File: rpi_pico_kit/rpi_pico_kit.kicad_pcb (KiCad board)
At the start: 2 copper layers, 99.1 x 99.1 mm, 195 parts, among them J1 DC Jack 5.5x2.1mm, J10 OLED Display SSD1306, J11 Conn_01x04_Male, J12 Conn_01x04_Male, J13 AudioJack-CUI-SJ-3523-SMT, J14 AudioJack-CUI-SJ-3523-SMT, J2 USB_B, J3 Conn_01x03_Male, J4 DB15_Female, J5 HDMI_A, J6 Conn_01x08_Male, J7 Conn_01x08_Male, J8 Conn_01x08_Male, J9 Micro_SD_Card_Det, Q1 DMN63D8L-7, Q2 DMN63D8L-7, Q3 DMN63D8L-7, Q4 DMN63D8L-7, Q5 DMN63D8L-7, Q6 DMN63D8L-7, Q7 DMN63D8L-7, SW1 SW_Push, SW10 SW_Push, SW2 RotaryEncoder_Switch, SW3 SW_Push, SW4 SW_Push, SW5 SW_Push, SW6 SW_Push, SW7 SW_Push, SW8 SW_Push, SW9 SW_Push, U1 RPi Pico, U10 74LVC2G34GV, U11 PCM5101A, U2 NCP1117-3.3_SOT223, U3 RP2040, U4 W25Q16JVSSIQ, U5 74HC14, U6 74HC14, U7 MCP23S08-xSO, U8 AT24CS32, U9 NCP115-3.3_SOT23-5, Y1 12MHz

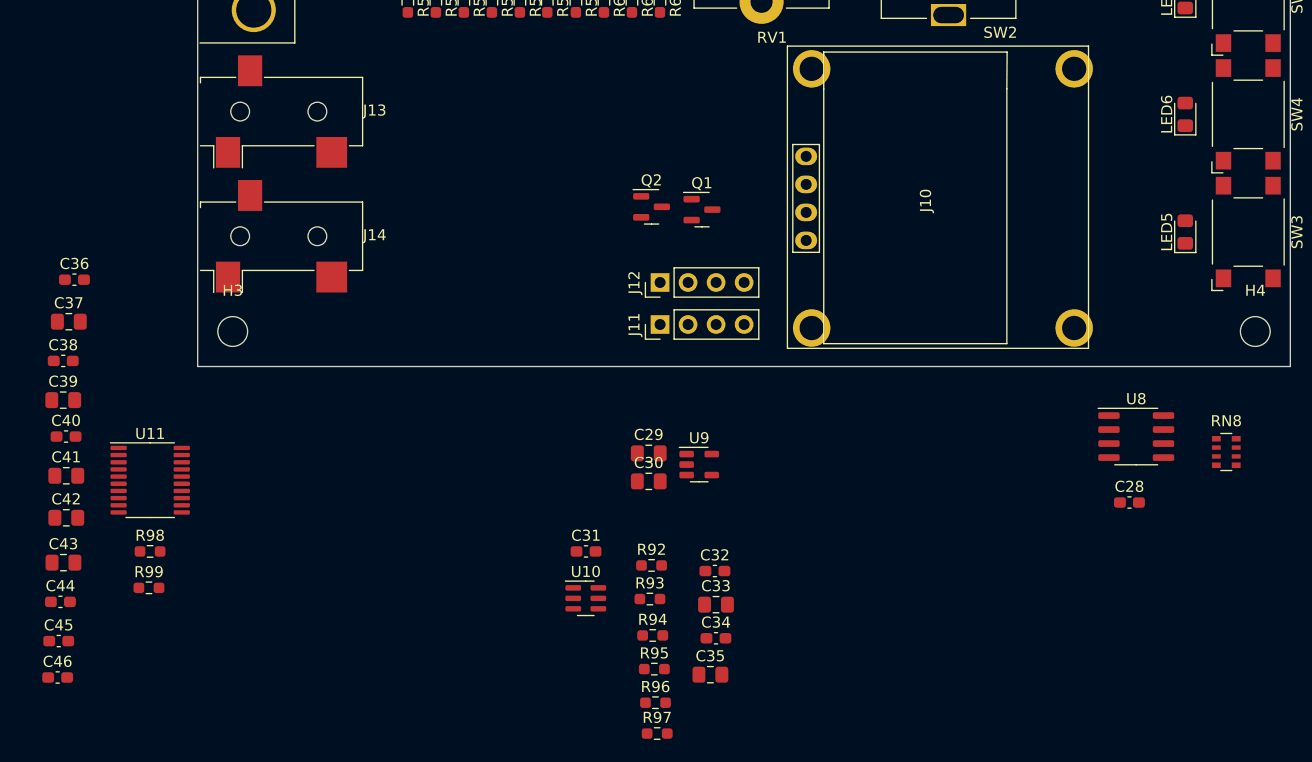
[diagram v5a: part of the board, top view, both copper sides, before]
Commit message: replaced audio
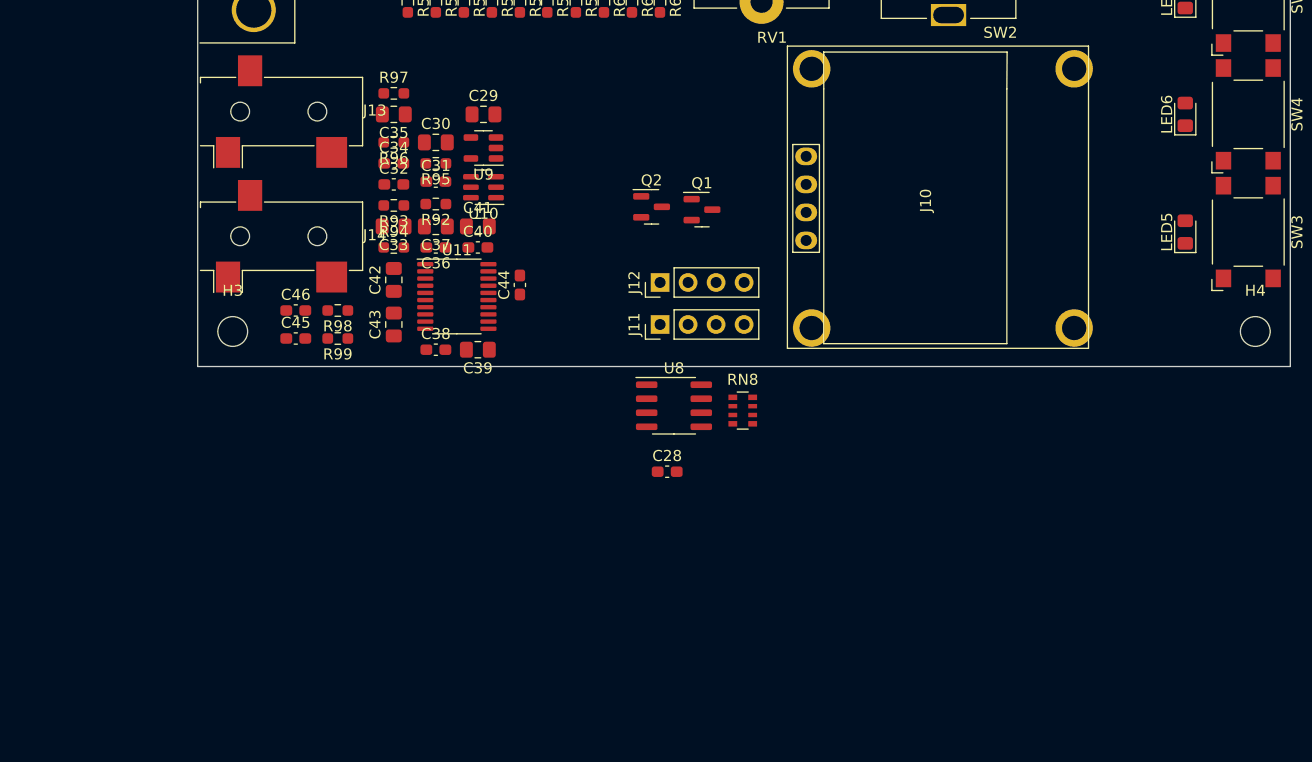
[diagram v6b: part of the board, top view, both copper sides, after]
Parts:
- moved R97 62.8 mm to (55.9, 112.4)
- moved C35 58.3 mm to (55.9, 114.3), turned to 180 degrees
- moved R96 56.1 mm to (55.9, 116.8), turned to 180 degrees
- moved C34 52.0 mm to (55.9, 118.7)
- moved C44 50.6 mm to (67.3, 129.8), turned to 90 degrees
- moved R95 49.9 mm to (59.7, 118.7), turned to 180 degrees
- moved C32 45.6 mm to (55.9, 120.7)
- moved C33 45.1 mm to (55.9, 124.5), turned to 180 degrees
- moved RN8 44.0 mm to (87.5, 141.2)
- moved C41 43.6 mm to (63.5, 124.5)
- moved R93 42.6 mm to (55.9, 122.6), turned to 180 degrees
- moved R94 42.3 mm to (55.9, 126.4)
- moved C28 42.0 mm to (80.7, 146.7)
- moved U8 42.0 mm to (81.3, 140.7)
- moved C40 41.1 mm to (63.5, 126.4)
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
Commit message: 4 layer stackup
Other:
- copper layers 2 -> 4
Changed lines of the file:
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@@
 (kicad_pcb (version 20220211) (generator pcbnew)
   (general
-    (thickness 0)
+    (thickness 4.69)
   )
   (paper "A4")
   (layers
     (0 "F.Cu" signal)
+    (1 "In1.Cu" signal)
+    (2 "In2.Cu" signal)
     (31 "B.Cu" signal)
     (32 "B.Adhes" user "B.Adhesive")
@@
   )
   (setup
+    (stackup
+      (layer "F.SilkS" (type "Top Silk Screen"))
+      (layer "F.Paste" (type "Top Solder Paste"))
+      (layer "F.Mask" (type "Top Solder Mask") (thickness 0.01))
+      (layer "F.Cu" (type "copper") (thickness 0.035))
+      (layer "dielectric 1" (type "core") (thickness 1.51) (material "FR4") (epsilon_r 4.5) (loss_tangent 0.02))
+      (layer "In1.Cu" (type "copper") (thickness 0.035))
+      (layer "dielectric 2" (type "prepreg") (thickness 1.51) (material "FR4") (epsilon_r 4.5) (loss_tangent 0.02))
+      (layer "In2.Cu" (type "copper") (thickness 0.035))
+      (layer "dielectric 3" (type "core") (thickness 1.51) (material "FR4") (epsilon_r 4.5) (loss_tangent 0.02))
+      (layer "B.Cu" (type "copper") (thickness 0.035))
+      (layer "B.Mask" (type "Bottom Solder Mask") (thickness 0.01))
+      (layer "B.Paste" (type "Bottom Solder Paste"))
+      (layer "B.SilkS" (type "Bottom Silk Screen"))
+      (copper_finish "None")
+      (dielectric_constraints no)
+    )
     (pad_to_mask_clearance 0.05)
     (pcbplotparams
